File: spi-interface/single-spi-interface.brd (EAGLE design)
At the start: 39.6 x 52.7 mm, 104 parts, among them Q1 AO3402, Q2 AO3402, U1 LY3200, U2 LY3200, U3 LY3200, U4 ADXL335

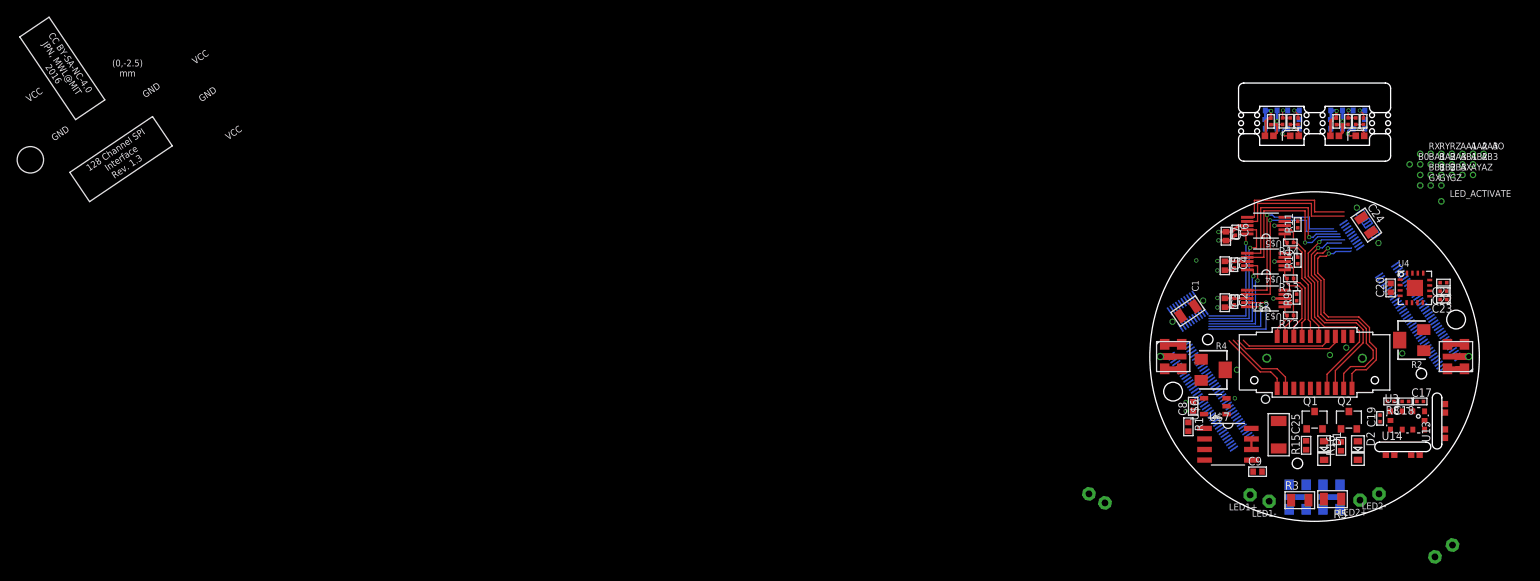
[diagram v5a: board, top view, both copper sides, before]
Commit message: Nearly finished with SPI inteface.
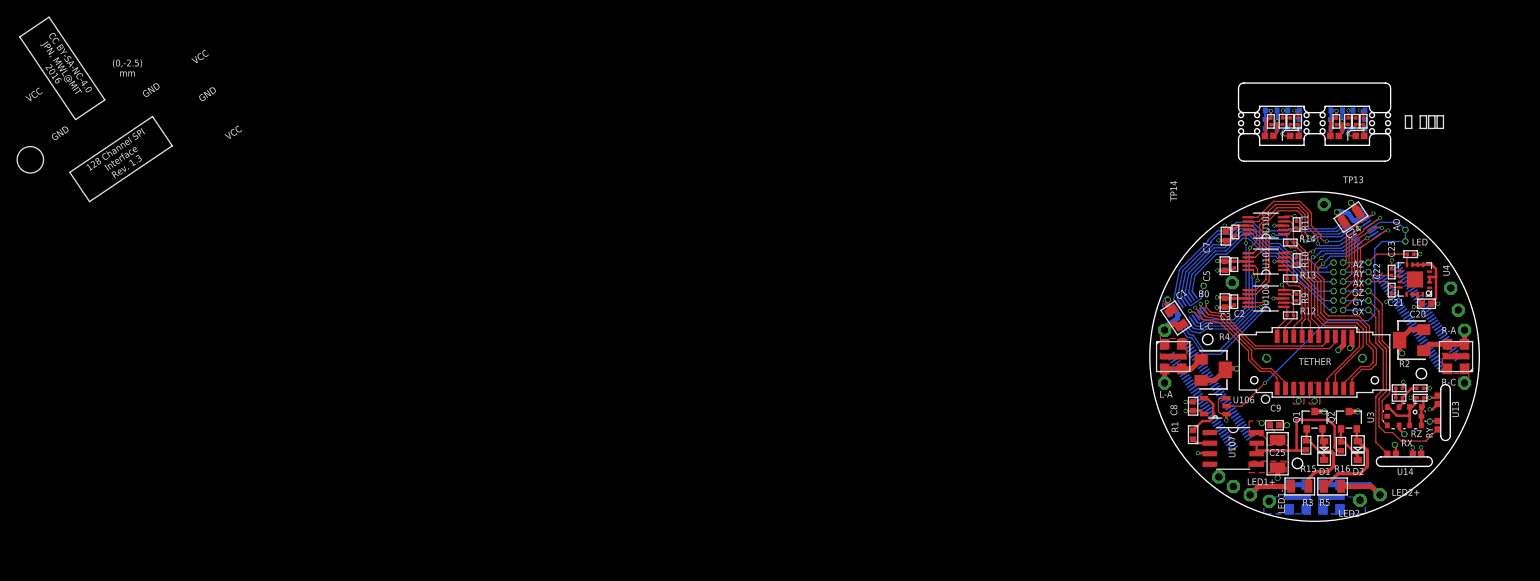
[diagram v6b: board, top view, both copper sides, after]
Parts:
- removed ANT: MLE-V01, jonnew:LED-MLE
- removed LED_ACTIVATE: (no value), jonnew:TESTPOINT_0.5MM
- removed POST: MLE-T01, jonnew:LED-MLE
- removed U$2: (no value), jonnew:T1M-10-T-DV
- removed U$3, U$4, U$5: MAX9174_UMAX, jonnew:10-UMAX
- removed U$6: NC7SZ125, jonnew:SOT-23-5
- removed U$7: SI822X, jonnew:SOIC127P500X400-8N
- added L-A, L-C, R-A, R-C, TP13, TP14: (no value), jonnew:TESTPOINT_SMALL
- added LED: (no value), jonnew:TESTPOINT_0.5MM
- added LEFT: MLE-T01, jonnew:LED-MLE
- added RIGHT: MLE-V01, jonnew:LED-MLE
- added TETHER: (no value), jonnew:T1M-10-T-DV
- added U100, U101, U102: MAX9174, jonnew:10-UMAX
- added U106: NC7SZ, jonnew:SOT-23-5
- added U107: SI822X, jonnew:SOIC127P500X400-8N
- D1: value PDZ10B,115 -> PDZ10B
- moved RX 35.1 mm to (9.65, -10.6)
- moved RZ 34.0 mm to (10.8, -9.33)
- moved TP2 32.4 mm to (16.4, 8.24), turned to 0 degrees
- moved RY 32.2 mm to (13.8, -7.81)
- moved B0 28.8 mm to (-13.3, 8.51), turned to 270 degrees
- moved TP6 28.3 mm to (17.3, 5.59), turned to 0 degrees
- moved AA1 22.9 mm to (3.43, 5.59)
- moved AA2 22.8 mm to (3.43, 6.73)
- moved AA3 22.7 mm to (3.43, 7.87)
- moved BA1 20.4 mm to (2.29, 5.59), turned to 270 degrees
- moved BA2 20.1 mm to (2.29, 6.73), turned to 270 degrees
- moved BA3 20.0 mm to (2.29, 7.87), turned to 270 degrees
- moved AB3 19.6 mm to (3.43, 11.3)
- moved AB2 19.3 mm to (3.43, 10.2)
- moved AB1 19.2 mm to (3.43, 9.02)
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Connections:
- net CS+: now also TETHER.20, U100.1; no longer U$2.20, U$3.1
- net CS+_HSA: now also U100.7; no longer U$3.7
- net CS+_HSB: now also U100.10; no longer U$3.10
- net CS-: now also TETHER.19, U100.2; no longer U$2.19, U$3.2
- net CS-_HSA: now also U100.6; no longer U$3.6
- net CS-_HSB: now also U100.9; no longer U$3.9
- net GND: now also L-C.1, LEFT.C1, LEFT.C2, LEFT.HS, R-C.1, RIGHT.C1, RIGHT.C2, RIGHT.HS, TETHER.11, TP13.1, TP14.1, U100.3, U101.3, U102.3, U106.1, U106.3, U107.3; no longer ANT.C1, ANT.C2, ANT.HS, POST.C1, POST.C2, POST.HS, U$2.11, U$3.3, U$4.3, U$5.3, U$6.1, U$6.3, U$7.3
- net MISO1+: now also TETHER.8; no longer U$2.8
- net MISO1-: now also TETHER.7; no longer U$2.7
- net MISO2+: now also TETHER.10; no longer U$2.10
- net MISO2-: now also TETHER.9; no longer U$2.9
- net MISO3+: now also TETHER.2; no longer U$2.2
- net MISO3-: now also TETHER.1; no longer U$2.1
- net MISO4+: now also TETHER.14; no longer U$2.14
- net MISO4-: now also TETHER.13; no longer U$2.13
- net MOSI+: now also TETHER.16, U102.1; no longer U$2.16, U$5.1
- net MOSI+_HSA: now also U102.7; no longer U$5.7
- net MOSI+_HSB: now also U102.10; no longer U$5.10
- net MOSI-: now also TETHER.15, U102.2; no longer U$2.15, U$5.2
- net MOSI-_HSA: now also U102.6; no longer U$5.6
- net MOSI-_HSB: now also U102.9; no longer U$5.9
- net N$1: now also U107.2; no longer U$7.2
- net N$13: now also L-A.1, LEFT.A1, LEFT.A2; no longer POST.A1, POST.A2
- net N$17: now also U100.4; no longer U$3.4
- net N$18: now also U102.4; no longer U$5.4
- net N$19: now also U101.4; no longer U$4.4
- net N$22: now also U107.6, U107.7; no longer U$7.6, U$7.7
- net N$5: now also LED.1, U106.2; no longer LED_ACTIVATE.1, U$6.2
- net N$6: now also U106.4; no longer U$6.4
- net N$9: now also R-A.1, RIGHT.A1, RIGHT.A2; no longer ANT.A1, ANT.A2
- net SCLK+: now also TETHER.18, U101.1; no longer U$2.18, U$4.1
- net SCLK+_HSA: now also U101.7; no longer U$4.7
- net SCLK+_HSB: now also U101.10; no longer U$4.10
- net SCLK-: now also TETHER.17, U101.2; no longer U$2.17, U$4.2
- net SCLK-_HSA: now also U101.6; no longer U$4.6
- net SCLK-_HSB: now also U101.9; no longer U$4.9
- net VCC: now also TETHER.12, U100.5, U100.8, U101.5, U101.8, U102.5, U102.8, U106.5; no longer U$2.12, U$3.5, U$3.8, U$4.5, U$4.8, U$5.5, U$5.8, U$6.5
- net VDD: now also TETHER.3, TETHER.4, U107.8; no longer U$2.3, U$2.4, U$7.8
- net VSS: now also TETHER.5, TETHER.6, U107.5; no longer U$2.5, U$2.6, U$7.5
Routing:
- net GND: track 33.9 -> 69.9 mm, vias 19 -> 24
- net VCC: track 22.4 -> 57.8 mm, vias 10 -> 17
- net N$5: track 0.00 -> 34.5 mm, vias 0 -> 1
- net AUXIN3_HSB_B: track 0.00 -> 28.1 mm
- net AUXIN2_HSB_B: track 0.00 -> 27.0 mm
- net AUXIN1_HSB_B: track 0.00 -> 26.4 mm
- net AUXIN3_HSB_A: track 0.00 -> 25.6 mm
- net AUXIN2_HSB_A: track 0.00 -> 25.1 mm
- net OUTY: track 0.00 -> 24.8 mm
- net AUXIN1_HSB_A: track 0.00 -> 24.5 mm
- net OUTX: track 0.00 -> 19.0 mm
- net N$22: track 1.27 -> 19.3 mm
- net OUTZ: track 0.00 -> 17.9 mm
- net AUXIN1_HSA_A: track 0.00 -> 14.0 mm, vias 0 -> 1
- net N$3: track 0.00 -> 12.6 mm
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- added copper zone on layer 1, net GND
- added copper zone on layer 1, net VDD
- added copper zone on layer 1, net VSS
- added copper zone on layer 16, net VSS
